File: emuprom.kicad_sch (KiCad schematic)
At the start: 34 parts, among them J1 Conn_02x20_Odd_Even, J2 Conn_02x03_Odd_Even, J3 USB_C_Receptacle_USB2.0_14P, J4 Conn_01x02, U1 CY62256-70PC, U10 74HC244, U11 74HC04, U2 74HC244, U3 74HC244, U4 74HC245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

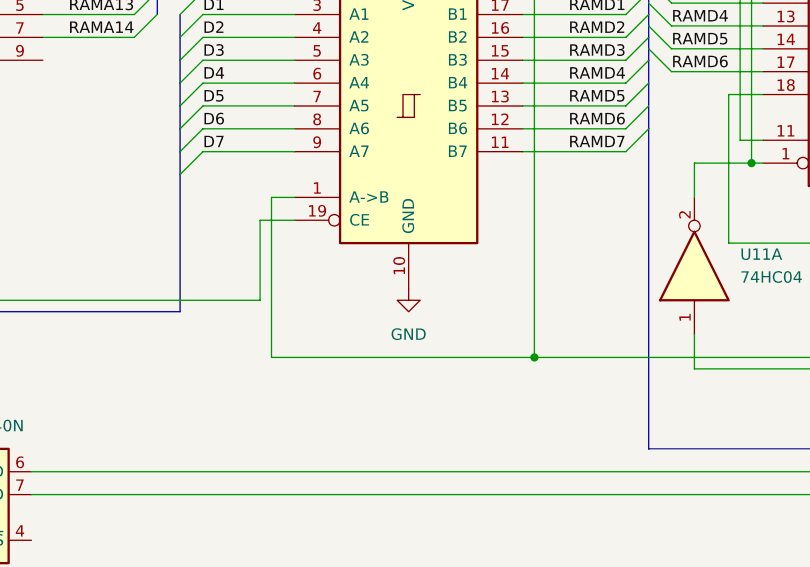
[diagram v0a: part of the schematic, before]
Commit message: Fix HW bug
U4 direction pin was tied to the wrong signal -
should be /RD instead of /WR. Tied it to the ground
instead. Now U4 74HC245 should be replaced with
74HC244, but it would require big layout change, so
I'm leaving it as is.
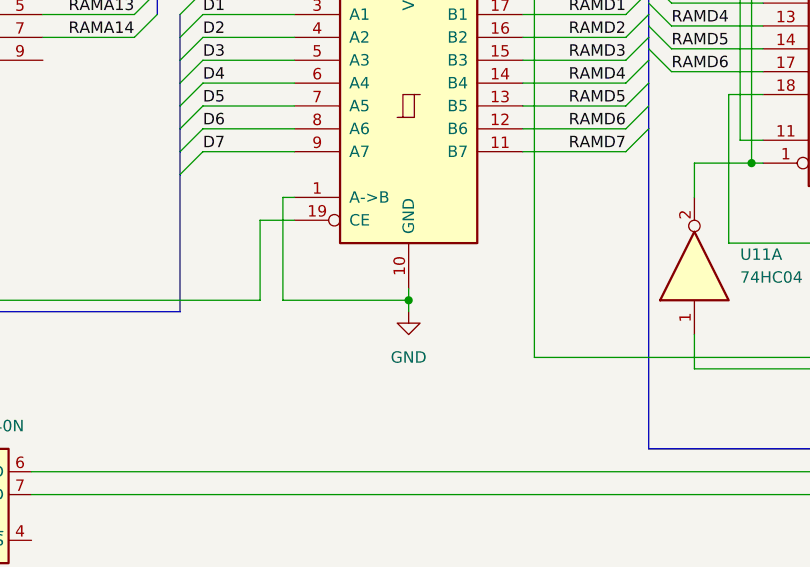
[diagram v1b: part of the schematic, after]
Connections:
- net GND: now also U4.1 (A->B)
- net at U1.27 (~{WE}), U6.25 (PC2): no longer U4.1 (A->B)
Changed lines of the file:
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@@
 	)
 	(junction
-		(at 187.96 187.96)
+		(at 173.99 181.61)
 		(diameter 0)
 		(color 0 0 0 0)
@@
 	(wire
 		(pts
+			(xy 173.99 181.61) (xy 173.99 180.34)
+		)
+		(stroke
+			(width 0)
+			(type default)
+		)
+	)
+	(wire
+		(pts
 			(xy 280.67 153.67) (xy 278.13 153.67)
 		)
@@
 		)
 	)
+	(wire
+		(pts
+			(xy 160.02 170.18) (xy 161.29 170.18)
+		)
+		(stroke
+			(width 0)
+			(type default)
+		)
+	)
 	(bus
 		(pts
@@
 	(wire
 		(pts
-			(xy 158.75 187.96) (xy 187.96 187.96)
-		)
-		(stroke
-			(width 0)
-			(type default)
-		)
-	)
-	(wire
-		(pts
 			(xy 120.65 171.45) (xy 105.41 171.45)
 		)
@@
 	(wire
 		(pts
-			(xy 158.75 170.18) (xy 158.75 187.96)
+			(xy 293.37 142.24) (xy 325.12 142.24)
 		)
 		(stroke
@@
 	(wire
 		(pts
-			(xy 293.37 142.24) (xy 325.12 142.24)
+			(xy 106.68 181.61) (xy 157.48 181.61)
 		)
 		(stroke
@@
 	(wire
 		(pts
-			(xy 106.68 181.61) (xy 157.48 181.61)
+			(xy 100.33 106.68) (xy 107.95 106.68)
 		)
 		(stroke
@@
 		)
 	)
-	(wire
+	(bus
 		(pts
-			(xy 100.33 106.68) (xy 107.95 106.68)
+			(xy 148.59 88.9) (xy 148.59 86.36)
 		)
 		(stroke
@@
 		)
 	)
-	(bus
+	(wire
 		(pts
-			(xy 148.59 88.9) (xy 148.59 86.36)
+			(xy 151.13 157.48) (xy 161.29 157.48)
 		)
 		(stroke
@@
 	(wire
 		(pts
-			(xy 151.13 157.48) (xy 161.29 157.48)
+			(xy 160.02 181.61) (xy 160.02 170.18)
 		)
 		(stroke
@@
 	(wire
 		(pts
+			(xy 173.99 182.88) (xy 173.99 181.61)
+		)
+		(stroke
+			(width 0)
+			(type default)
+		)
+	)
+	(wire
+		(pts
 			(xy 248.92 143.51) (xy 238.76 143.51)
 		)
@@
 	(wire
 		(pts
+			(xy 173.99 181.61) (xy 160.02 181.61)
+		)
+		(stroke
+			(width 0)
+			(type default)
+		)
+	)
+	(wire
+		(pts
 			(xy 156.21 30.48) (xy 160.02 30.48)
 		)
@@
 	(wire
 		(pts
-			(xy 161.29 170.18) (xy 158.75 170.18)
-		)
-		(stroke
-			(width 0)
-			(type default)
-		)
-	)
-	(wire
-		(pts
 			(xy 255.27 19.05) (xy 78.74 19.05)
 		)
@@
 	(symbol
 		(lib_id "power:GND")
-		(at 173.99 180.34 0)
+		(at 173.99 182.88 0)
 		(unit 1)
 		(exclude_from_sim no)
@@
 		(fields_autoplaced yes)
 		(property "Reference" "#PWR05"
-			(at 173.99 186.69 0)
+			(at 173.99 189.23 0)
 			(effects
 				(font
@@
 		)
 		(property "Value" "GND"
-			(at 173.99 185.42 0)
+			(at 173.99 187.96 0)
 			(effects
 				(font
@@
 		)
 		(property "Footprint" ""
-			(at 173.99 180.34 0)
+			(at 173.99 182.88 0)
 			(effects
 				(font
@@
 		)
 		(property "Datasheet" ""
-			(at 173.99 180.34 0)
+			(at 173.99 182.88 0)
 			(effects
 				(font
@@
 		)
 		(property "Description" "Power symbol creates a global label with name \"GND\" , ground"
-			(at 173.99 180.34 0)
+			(at 173.99 182.88 0)
 			(effects
 				(font

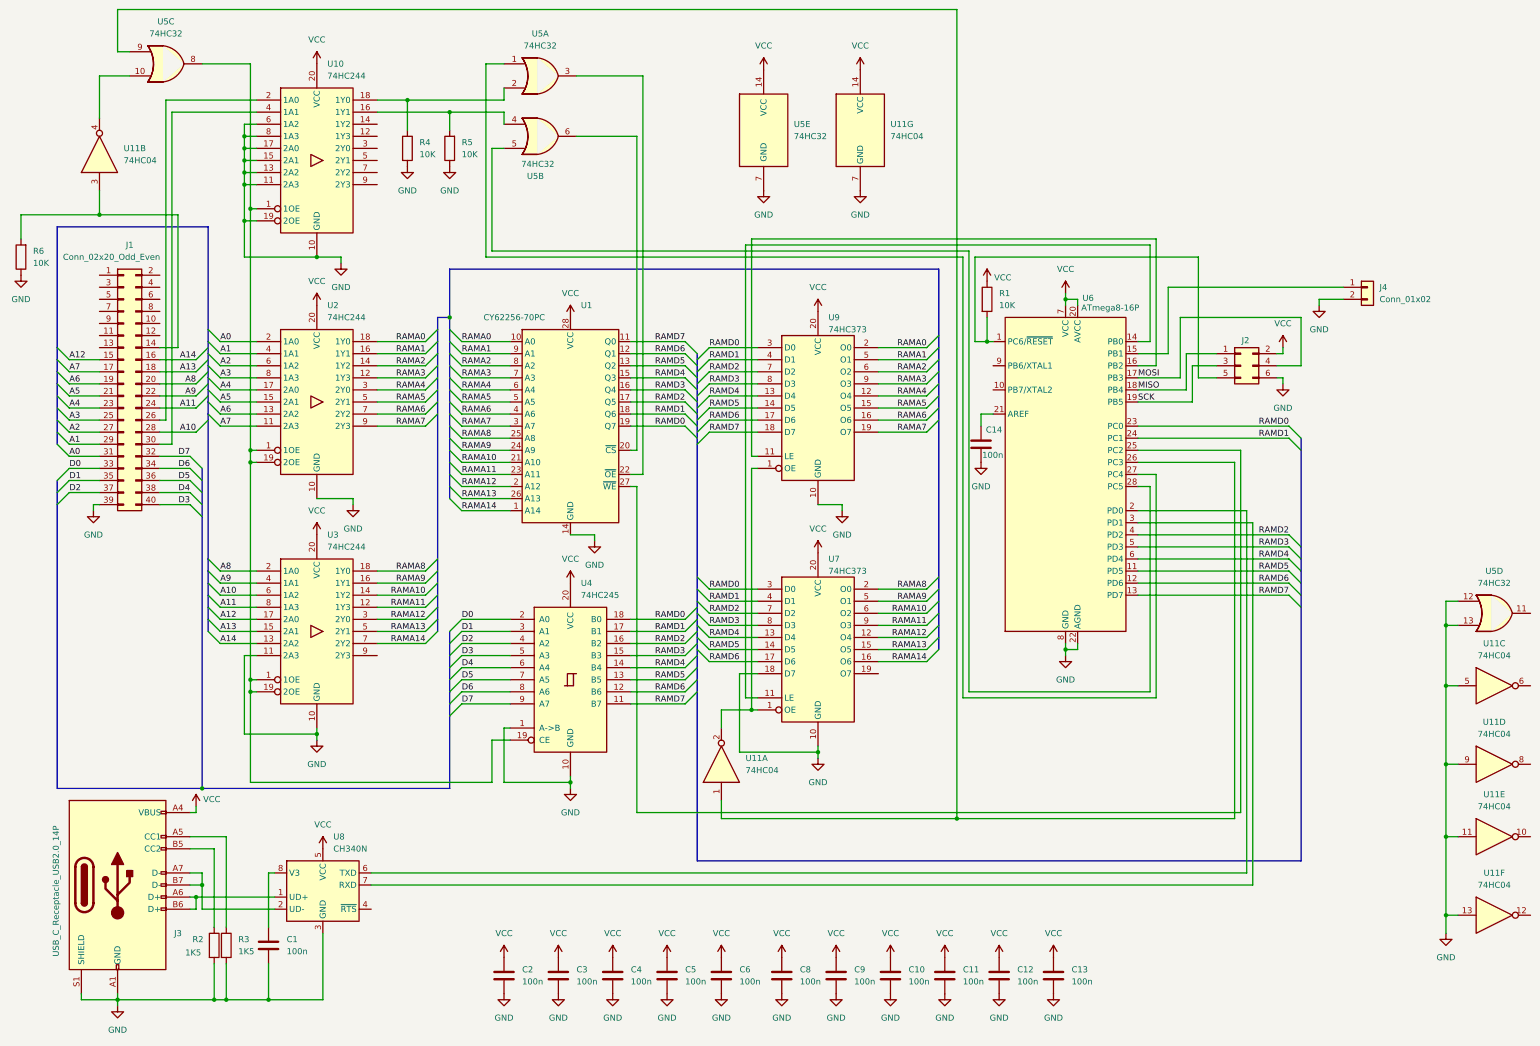
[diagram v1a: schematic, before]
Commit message: Revision C: redesign to fix U4 problem
Reduced PCB footprint slightly, change U11 74HC04 -> 74HC02
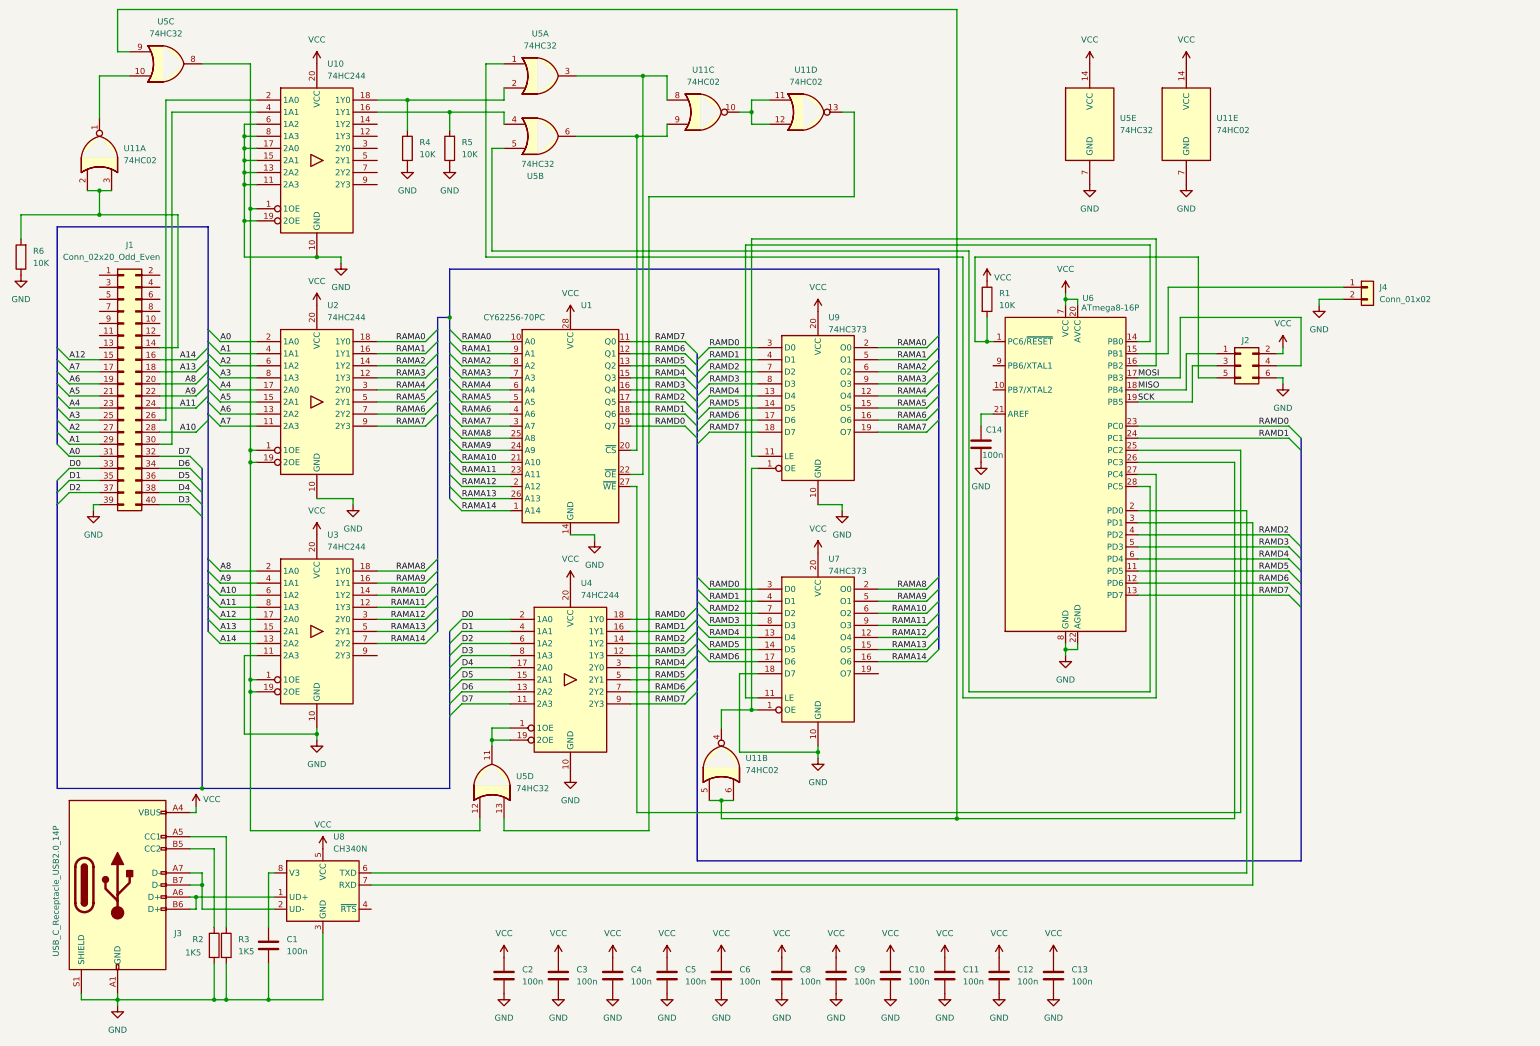
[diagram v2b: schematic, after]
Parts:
- removed U11: 74HC04, Package_DIP:DIP-14_W7.62mm, symbol 74xx:74HC04
- removed U4: 74HC245, Package_DIP:DIP-20_W7.62mm, symbol 74xx:74HC245
- added U11: 74HC02, Package_DIP:DIP-14_W7.62mm, symbol 74xx:74HC02
- added U4: 74HC244, Package_DIP:DIP-20_W7.62mm, symbol 74xx:74HC244
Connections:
- net D0: now also U4.2 (1A0)
- net D1: now also U4.4 (1A1)
- net D2: now also U4.6 (1A2)
- net D3: now also U4.8 (1A3)
- net D4: now also U4.17 (2A0)
- net D5: now also U4.15 (2A1)
- net D6: now also U4.13 (2A2)
- net D7: now also U4.11 (2A3)
- net GND: now also U11.7 (GND), U4.10 (GND); no longer U5.12, U5.13
- net RAMD0: now also U4.18 (1Y0)
- net RAMD1: now also U4.16 (1Y1)
- net RAMD2: now also U4.14 (1Y2)
- net RAMD3: now also U4.12 (1Y3)
- net RAMD4: now also U4.3 (2Y0)
- net RAMD5: now also U4.5 (2Y1)
- net RAMD6: now also U4.7 (2Y2)
- net RAMD7: now also U4.9 (2Y3)
- net VCC: now also U11.14 (VCC), U4.20 (VCC)
- net at U1.22 (~{OE}), U5.3: now also U11.8
- net at U10.1 (1OE), U2.1 (1OE), U2.19 (2OE)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: now also U5.12
- net at J1.14 (Pin_14), R6.2: now also U11.2, U11.3
- net at U1.20 (~{CS}), U5.6: now also U11.9
- net at U5.11: now also U4.1 (1OE), U4.19 (2OE)
- net at U5.9, U6.26 (PC3): now also U11.5, U11.6
- net at U7.1 (OE), U9.1 (OE): now also U11.4
- net at U5.10: now also U11.1
- new net: U11.13, U5.13
- new net: U11.10, U11.11, U11.12
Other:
- moved on the sheet: U5D, U5E

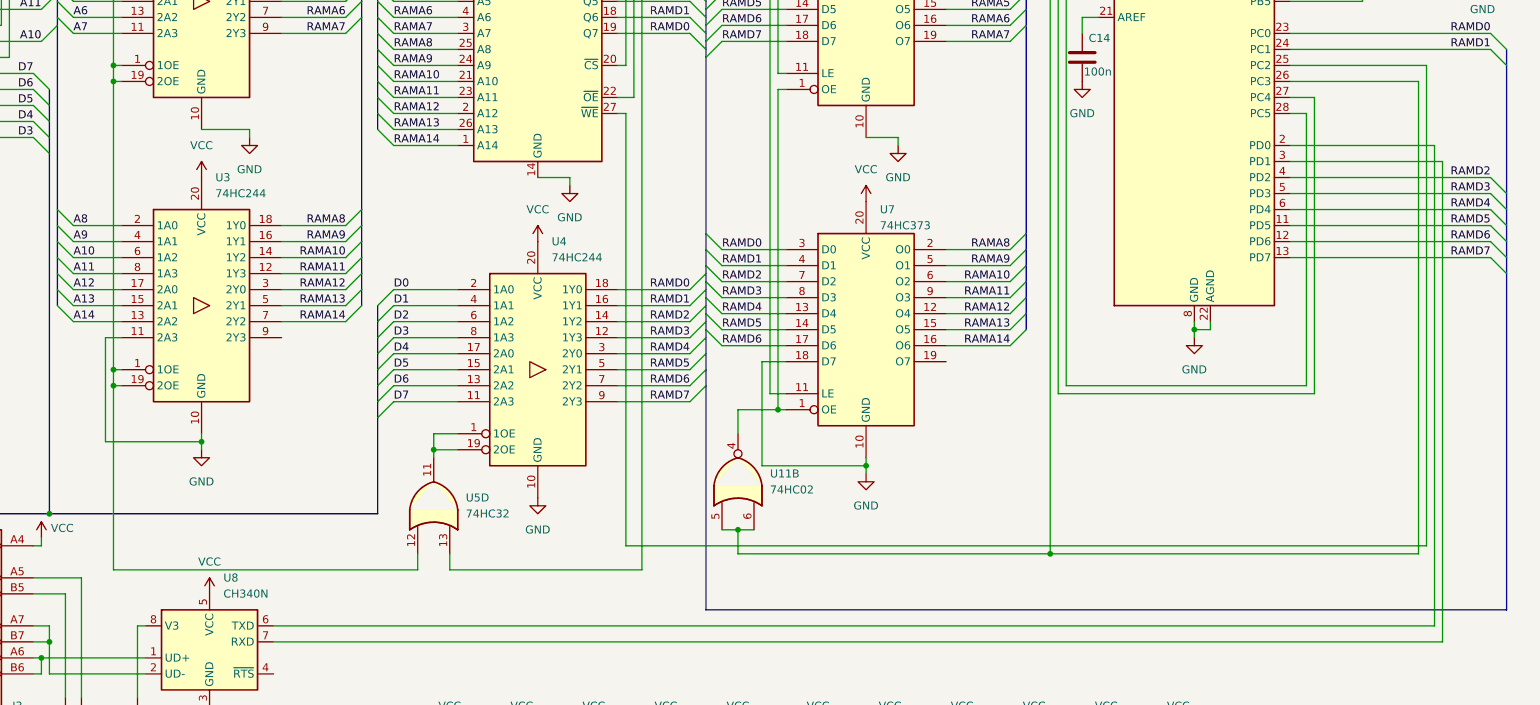
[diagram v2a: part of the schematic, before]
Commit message: rev D: Fix U4 output being swapped with input
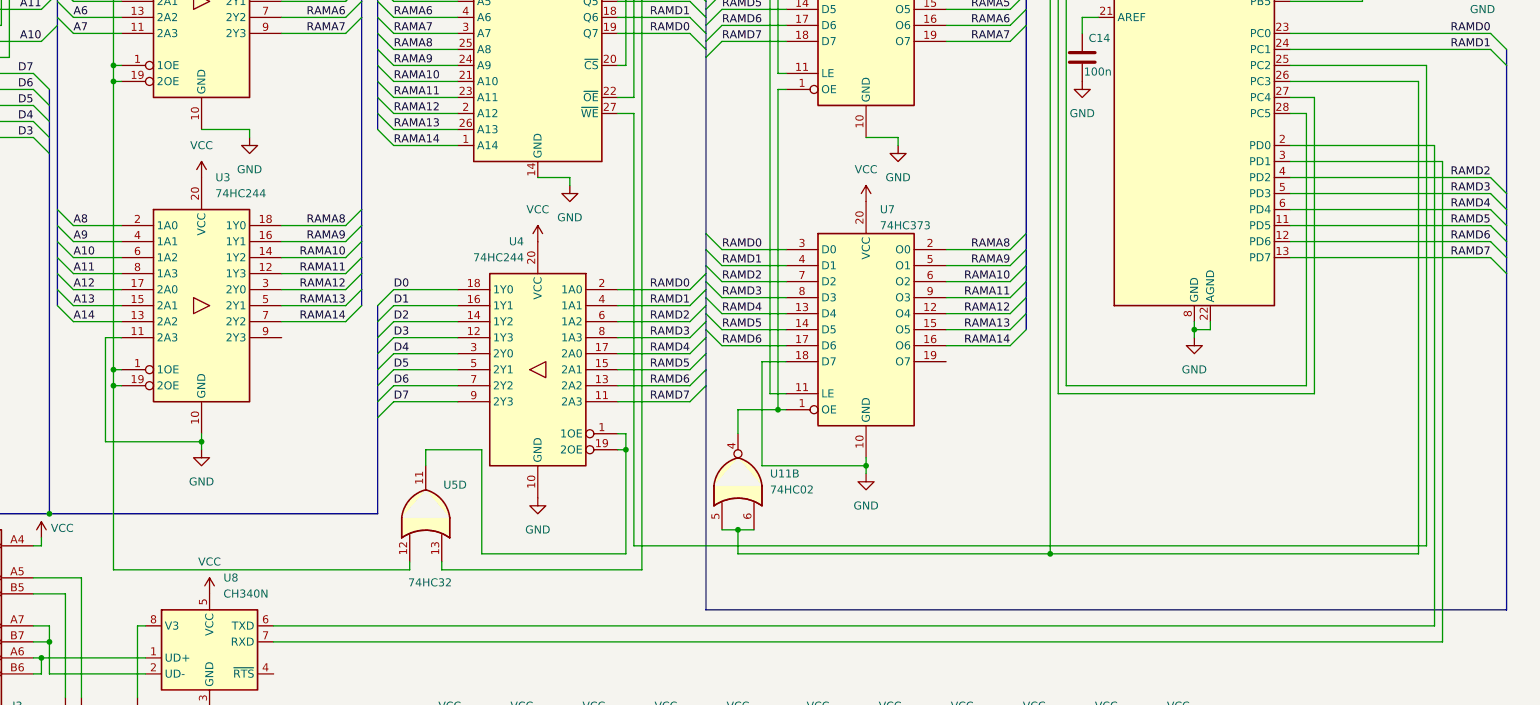
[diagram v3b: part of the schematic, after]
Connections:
- net D0: now also U4.18 (1Y0); no longer U4.2 (1A0)
- net D1: now also U4.16 (1Y1); no longer U4.4 (1A1)
- net D2: now also U4.14 (1Y2); no longer U4.6 (1A2)
- net D3: now also U4.12 (1Y3); no longer U4.8 (1A3)
- net D4: now also U4.3 (2Y0); no longer U4.17 (2A0)
- net D5: now also U4.5 (2Y1); no longer U4.15 (2A1)
- net D6: now also U4.7 (2Y2); no longer U4.13 (2A2)
- net D7: now also U4.9 (2Y3); no longer U4.11 (2A3)
- net RAMD0: now also U4.2 (1A0); no longer U4.18 (1Y0)
- net RAMD1: now also U4.4 (1A1); no longer U4.16 (1Y1)
- net RAMD2: now also U4.6 (1A2); no longer U4.14 (1Y2)
- net RAMD3: now also U4.8 (1A3); no longer U4.12 (1Y3)
- net RAMD4: now also U4.17 (2A0); no longer U4.3 (2Y0)
- net RAMD5: now also U4.15 (2A1); no longer U4.5 (2Y1)
- net RAMD6: now also U4.13 (2A2); no longer U4.7 (2Y2)
- net RAMD7: now also U4.11 (2A3); no longer U4.9 (2Y3)
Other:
- moved on the sheet: U5D
